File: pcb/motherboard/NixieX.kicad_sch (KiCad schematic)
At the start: 12 parts, among them Q4 MPSA42, Q5 MPSA42, Q6 MPSA42, Q7 MPSA42

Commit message: Ver 3.0
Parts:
- removed R22, R23: 47k, Resistor_THT:R_Axial_DIN0204_L3.6mm_D1.6mm_P2.54mm_Vertical, symbol Device:R_Small
- added Q10, Q11, Q8, Q9: S8050, Package_TO_SOT_THT:TO-92_Inline, symbol Transistor_BJT:S8050
- added R18, R19: 47k, Resistor_THT:R_Axial_DIN0204_L3.6mm_D1.6mm_P5.08mm_Horizontal, symbol Device:R_Small
- R14: renamed from R16; footprint Resistor_THT:R_Axial_DIN0204_L3.6mm_D1.6mm_P2.54mm_Vertical -> Resistor_THT:R_Axial_DIN0309_L9.0mm_D3.2mm_P12.70mm_Horizontal
- R15: renamed from R17; footprint Resistor_THT:R_Axial_DIN0204_L3.6mm_D1.6mm_P2.54mm_Vertical -> Resistor_THT:R_Axial_DIN0309_L9.0mm_D3.2mm_P12.70mm_Horizontal
- R16: renamed from R18; footprint Resistor_THT:R_Axial_DIN0204_L3.6mm_D1.6mm_P2.54mm_Vertical -> Resistor_THT:R_Axial_DIN0309_L9.0mm_D3.2mm_P12.70mm_Horizontal
- R17: renamed from R19; footprint Resistor_THT:R_Axial_DIN0204_L3.6mm_D1.6mm_P2.54mm_Vertical -> Resistor_THT:R_Axial_DIN0309_L9.0mm_D3.2mm_P12.70mm_Horizontal
- R20, R21: footprint Resistor_THT:R_Axial_DIN0204_L3.6mm_D1.6mm_P2.54mm_Vertical -> Resistor_THT:R_Axial_DIN0204_L3.6mm_D1.6mm_P5.08mm_Horizontal
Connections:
- net +170V: now also R15.2; no longer R15.1
- net GND: now also Q10.1 (E), Q11.1 (E), Q8.1 (E), Q9.1 (E)
- net IN_P0: now also Q8.2 (B); no longer R20.1
- net IN_P1: now also Q9.2 (B); no longer R21.1
- net IN_P2: now also Q10.2 (B)
- net IN_P3: now also Q11.2 (B)
- net OUT_P3: now also R15.1; no longer R15.2
- net at Q5.2 (B): now also Q9.3 (C), R18.2; no longer R21.2
- net at Q4.2 (B), R20.2: now also Q8.3 (C)
- net at Q7.2 (B): now also Q11.3 (C), R19.2
- net at Q6.2 (B): now also R21.2, Q10.3 (C)
- new net +5V: R18.1, R19.1, R20.1, R21.1
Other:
- moved on the sheet: Q4, Q5, Q6, Q7, R14, R15, R16, R17

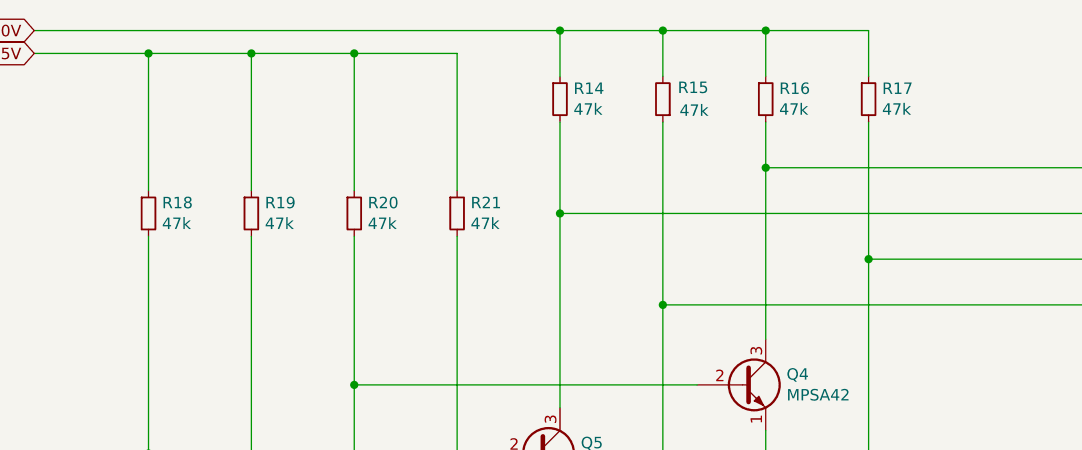
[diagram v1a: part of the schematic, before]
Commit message: Update resistor value
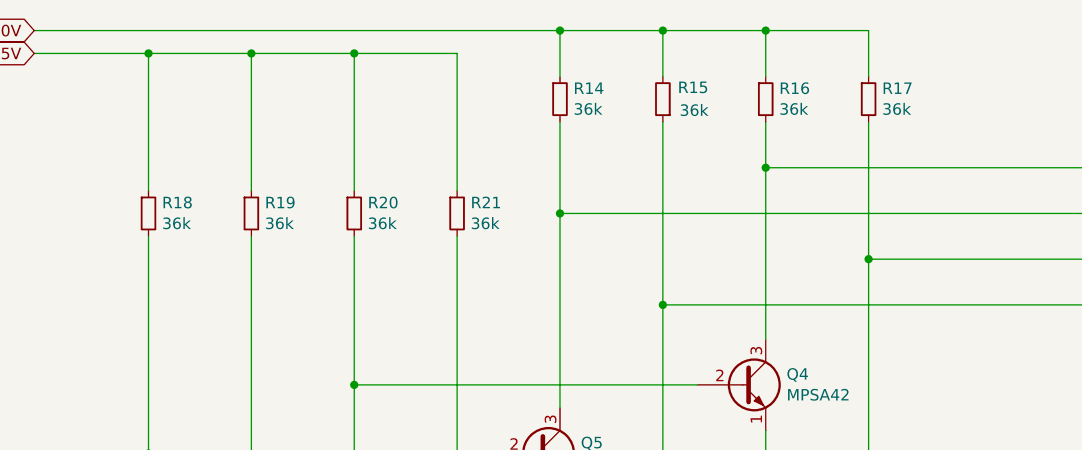
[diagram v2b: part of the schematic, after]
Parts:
- R14, R15, R16, R17, R18, R19, R20, R21: value 47k -> 36k
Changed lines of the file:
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@@
       (effects (font (size 1.27 1.27)) (justify left))
     )
-    (property "Value" "47k" (at 148.8186 46.863 0)
+    (property "Value" "36k" (at 148.8186 46.863 0)
       (effects (font (size 1.27 1.27)) (justify left))
     )
@@
       (effects (font (size 1.27 1.27)) (justify left))
     )
-    (property "Value" "47k" (at 163.83 46.99 0)
+    (property "Value" "36k" (at 163.83 46.99 0)
       (effects (font (size 1.27 1.27)) (justify left))
     )
@@
       (effects (font (size 1.27 1.27)) (justify left))
     )
-    (property "Value" "47k" (at 171.6786 46.863 0)
+    (property "Value" "36k" (at 171.6786 46.863 0)
       (effects (font (size 1.27 1.27)) (justify left))
     )
@@
       (effects (font (size 1.27 1.27)) (justify left))
     )
-    (property "Value" "47k" (at 183.1086 46.863 0)
+    (property "Value" "36k" (at 183.1086 46.863 0)
       (effects (font (size 1.27 1.27)) (justify left))
     )
@@
       (effects (font (size 1.27 1.27)) (justify left))
     )
-    (property "Value" "47k" (at 137.3886 59.563 0)
+    (property "Value" "36k" (at 137.3886 59.563 0)
       (effects (font (size 1.27 1.27)) (justify left))
     )
@@
       (effects (font (size 1.27 1.27)) (justify left))
     )
-    (property "Value" "47k" (at 103.0986 59.563 0)
+    (property "Value" "36k" (at 103.0986 59.563 0)
       (effects (font (size 1.27 1.27)) (justify left))
     )
@@
       (effects (font (size 1.27 1.27)) (justify left))
     )
-    (property "Value" "47k" (at 125.9586 59.563 0)
+    (property "Value" "36k" (at 125.9586 59.563 0)
       (effects (font (size 1.27 1.27)) (justify left))
     )
@@
       (effects (font (size 1.27 1.27)) (justify left))
     )
-    (property "Value" "47k" (at 114.5286 59.563 0)
-      (effects (font (size 1.27 1.27)) (justify left))
-    )
+    (property "Value" "36k" (at 114.5286 59.563 0)
+      (effects (font (size 1.27 1.27)) (justify left))
+    )
